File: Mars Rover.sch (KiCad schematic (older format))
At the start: 37 parts, among them J1 Barrel_Jack, SW1 KILLSWITCH

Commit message: Testing Commit
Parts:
- added D?: D_Schottky, symbol Device:D_Schottky
- added R?: R, symbol Device:R
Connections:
- net labels added: CHRG_VL
- wire segments 113 -> 115
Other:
- moved on the sheet: D?
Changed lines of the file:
@@
 Wire Wire Line
 	-5200 6100 -6300 6100
-Wire Wire Line
-	-5100 6050 -6500 6050
-Wire Wire Line
-	-6500 6050 -6500 6100
 $Comp
 L power:GND #PWR?
@@
 	-6300 6100 -6300 6450
 Connection ~ -6550 6450
-Wire Wire Line
-	-6500 5950 -6500 6050
-Connection ~ -6500 6050
 $Comp
 L Device:R R?
@@
 Connection ~ -2050 5200
 Wire Wire Line
-	-7350 4800 -2050 4800
-Wire Wire Line
 	-4100 5200 -2600 5200
 $Comp
@@
 L pspice:DIODE D?
 U 1 1 5C0E81FE
-P -3750 5550
-F 0 "D?" H -3750 5815 50  0000 C CNN
-F 1 "DIODE" H -3750 5724 50  0000 C CNN
-F 2 "" H -3750 5550 50  0001 C CNN
-F 3 "~" H -3750 5550 50  0001 C CNN
-	1    -3750 5550
-	1    0    0    -1
-$EndComp
-Wire Wire Line
-	-4100 5550 -3950 5550
+P -3600 5550
+F 0 "D?" H -3600 5815 50  0000 C CNN
+F 1 "DIODE" H -3600 5724 50  0000 C CNN
+F 2 "" H -3600 5550 50  0001 C CNN
+F 3 "~" H -3600 5550 50  0001 C CNN
+	1    -3600 5550
+	1    0    0    -1
+$EndComp
+Wire Wire Line
+	-4100 5550 -3800 5550
 $Comp
 L Device:C C?
@@
 Connection ~ -4000 6100
 Wire Wire Line
-	-3550 5550 -3400 5550
-Wire Wire Line
 	-3400 5550 -3400 5650
 Wire Wire Line
@@
 	-3750 6100 -3750 6850
 Wire Wire Line
-	-4000 6100 -3750 6100
+	-4000 6100 -3800 6100
 Wire Wire Line
 	-3750 6850 -3400 6850
@@
 Wire Wire Line
 	-2400 6950 -2400 6850
+Wire Wire Line
+	-6500 5950 -6500 6100
+Text Label -5450 6050 0    50   ~ 0
+CHRG_VL
+Wire Wire Line
+	-5100 6050 -5450 6050
+Text Label -4100 5550 0    50   ~ 0
+CHRG_VL
+Wire Wire Line
+	-7400 4800 -2050 4800
+$Comp
+L Device:D_Schottky D?
+U 1 1 5C0B3BF5
+P -3800 6250
+F 0 "D?" H -3800 6034 50  0000 C CNN
+F 1 "D_Schottky" H -3800 6125 50  0000 C CNN
+F 2 "" H -3800 6250 50  0001 C CNN
+F 3 "~" H -3800 6250 50  0001 C CNN
+	1    -3800 6250
+	0    1    1    0
+$EndComp
+Connection ~ -3800 6100
+Wire Wire Line
+	-3800 6100 -3750 6100
+Wire Wire Line
+	-4100 6350 -4100 6400
+Wire Wire Line
+	-4100 6400 -3850 6400
+$Comp
+L power:GND #PWR?
+U 1 1 5C0B7E2F
+P -3850 6400
+F 0 "#PWR?" H -3850 6150 50  0001 C CNN
+F 1 "GND" H -3845 6227 50  0000 C CNN
+F 2 "" H -3850 6400 50  0001 C CNN
+F 3 "" H -3850 6400 50  0001 C CNN
+	1    -3850 6400
+	1    0    0    -1
+$EndComp
+Connection ~ -3850 6400
+Wire Wire Line
+	-3850 6400 -3800 6400
+$Comp
+L Device:R R?
+U 1 1 5C0B8E08
+P -5700 2350
+F 0 "R?" H -5630 2396 50  0000 L CNN
+F 1 "R" H -5630 2305 50  0000 L CNN
+F 2 "" V -5770 2350 50  0001 C CNN
+F 3 "~" H -5700 2350 50  0001 C CNN
+	1    -5700 2350
+	1    0    0    -1
+$EndComp
 $EndSCHEMATC

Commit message: Battery Charger Done
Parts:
- added C?: 0.1uF, symbol Device:C
- C?: value CP1 -> 0.22uF
- C? (x2): value CP1 -> 22uF
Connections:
- net GND: now also C?.2
- net at U?.21 (CS): now also L?.2, C?.1

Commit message: Batteries done and raspi added
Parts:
- removed C? (x2): C, symbol Device:C
- removed C? (x7): 0.1uF, symbol Device:C
- removed C? (x3): 1nF, symbol Device:C
- removed C?: 1uF, symbol Device:C
- removed C?: CP1, symbol Device:CP1
- removed C?: 0.22uF, symbol Device:CP1
- removed C? (x2): 22uF, symbol Device:CP1
- removed D1, D2, D? (x2): D_Schottky, symbol Device:D_Schottky
- removed D? (x2): DIODE, symbol pspice:DIODE
- removed D? (x3): LED, symbol Device:LED
- removed L?: INDUCTOR, symbol pspice:INDUCTOR
- removed R? (x7): R, symbol Device:R
- removed R?: 10k, symbol Device:R
- removed R?: 0.05R, symbol Device:R
- removed U?: MAX1758, symbol Roverschemlib:MAX1758
- removed U?: Rpi0w, symbol Roverschemlib:Rpi0w
- added C?: 22uF, symbol Device:CP1
- added C?: 0.1uF, symbol Device:C
- added J?: Conn_01x03, symbol Connector_Generic:Conn_01x03
- added SW?: CHARGING, symbol Switch:SW_SPST
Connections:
- net +12V: now also SW?.2 (B); no longer SW1.1 (A)
- net GND: now also C?.1, C?.2
- net at J1.1: now also SW1.1 (A)
- net Buck5V/VIN renamed Battery Connection and Charge Management/VIN
- new net: C?.1, C?.2, J?.1 (Pin_1)
- new net Battery Connection and Charge Management/BATT_OUT: SW?.1 (A)
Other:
- note removed: "14.4V BATT IN HERE\n(PLUS CHARGING CKT)"
- note removed: "FASTCHG\n"
- note removed: "FAULT\n"
- note removed: "FULL CHARGE\n"
- note removed: "NOT 5VL, BUT ‘TO VL’"
- note removed: "VIN\n"
- note removed: "VOUT"
- moved on the sheet: J1, SW1

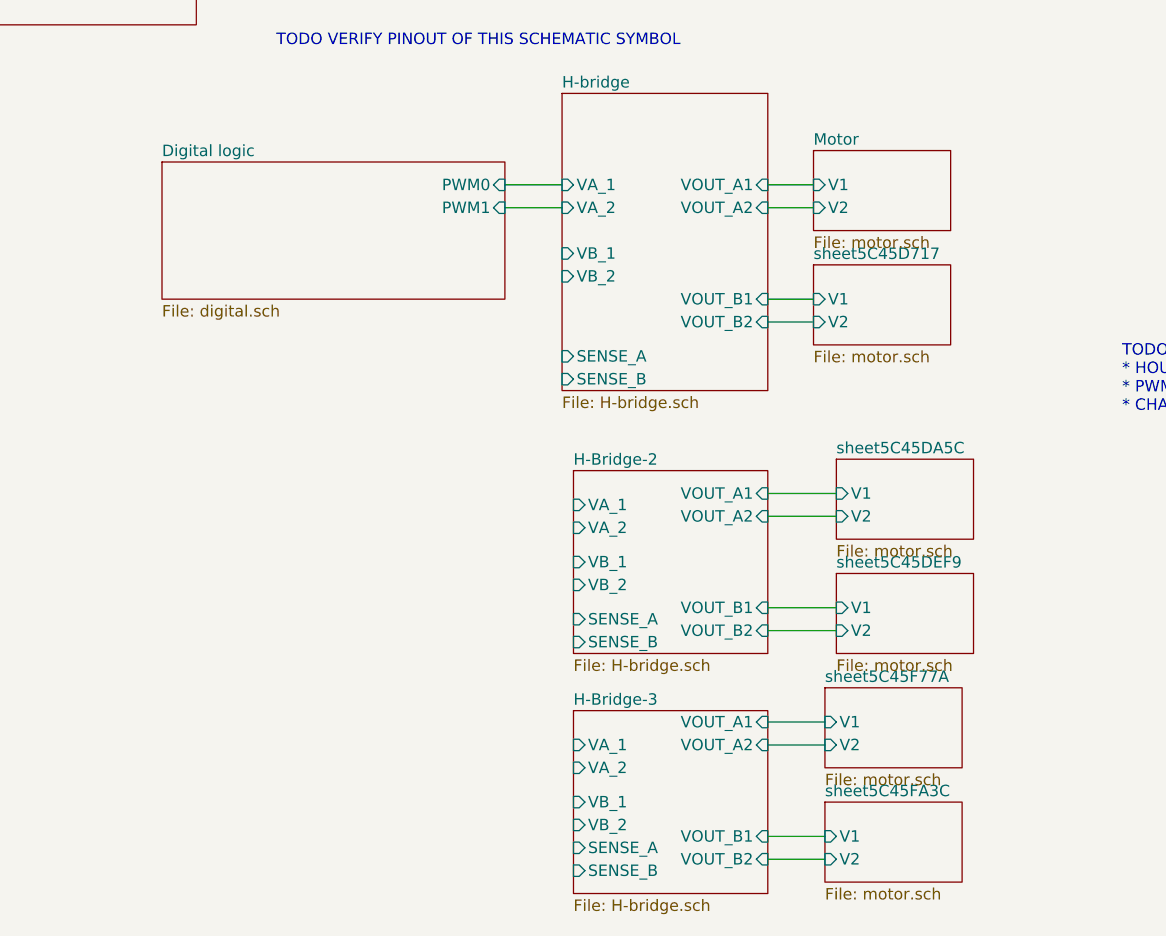
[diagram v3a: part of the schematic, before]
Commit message: Added housekeeping ADC, schematics almost done
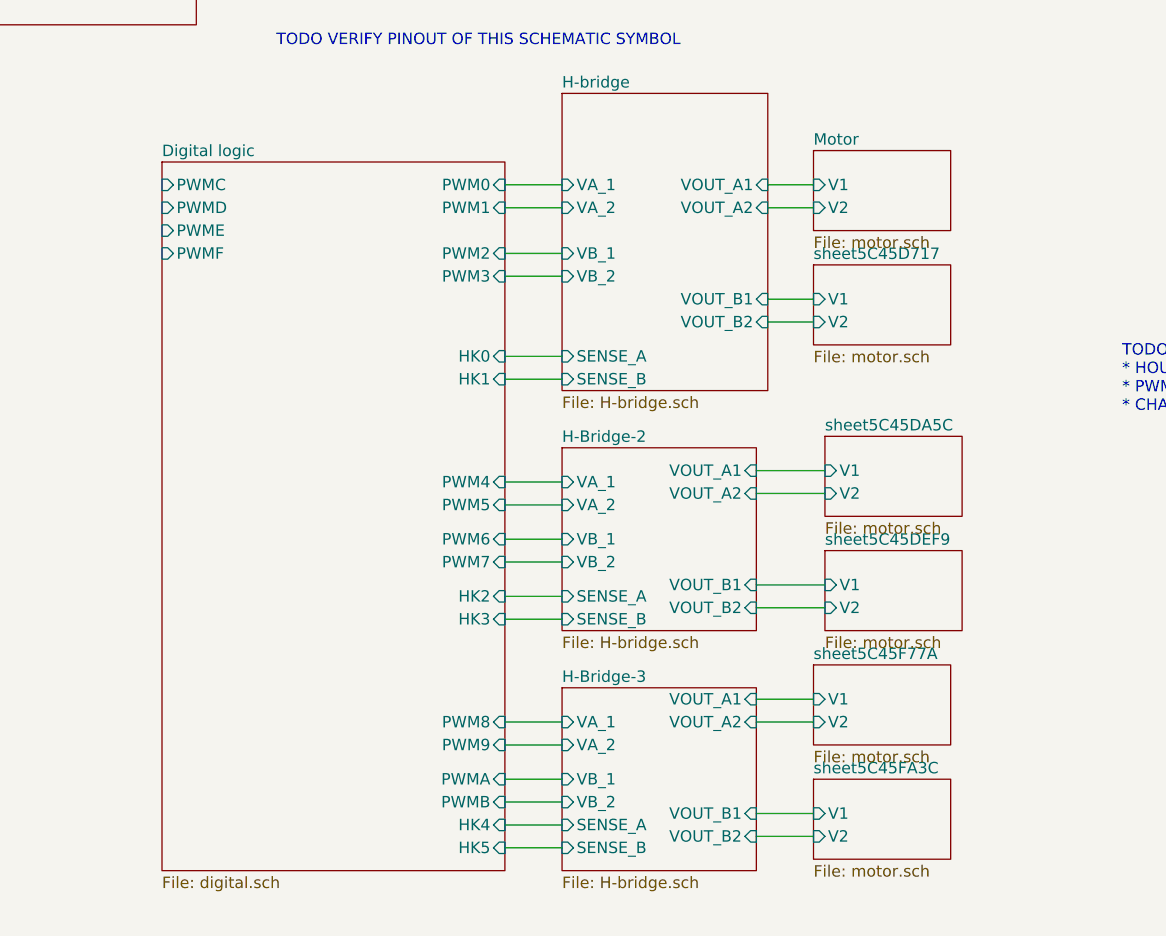
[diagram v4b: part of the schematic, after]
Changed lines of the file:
@@
 F0 "Motor" 50
 F1 "motor.sch" 50
-F3 "V1" I L 7000 3100 50
-F4 "V2" I L 7000 3200 50
-$EndSheet
-$Sheet
-S 5950 4350 850  800
+F2 "V1" I L 7000 3100 50
+F3 "V2" I L 7000 3200 50
+$EndSheet
+$Sheet
+S 5900 4250 850  800
 U 5BEEC4C8
 F0 "H-Bridge-2" 50
 F1 "H-bridge.sch" 50
-F2 "VOUT_B1" I R 6800 4950 50
-F3 "VOUT_B2" I R 6800 5050 50
-F4 "VOUT_A1" I R 6800 4450 50
-F5 "VOUT_A2" I R 6800 4550 50
-F6 "VB_1" I L 5950 4750 50
-F7 "VB_2" I L 5950 4850 50
-F8 "VA_1" I L 5950 4500 50
-F9 "VA_2" I L 5950 4600 50
-F10 "SENSE_B" I L 5950 5100 50
-F11 "SENSE_A" I L 5950 5000 50
-$EndSheet
-$Sheet
-S 5950 5400 850  800
+F2 "VOUT_B1" I R 6750 4850 50
+F3 "VOUT_B2" I R 6750 4950 50
+F4 "VOUT_A1" I R 6750 4350 50
+F5 "VOUT_A2" I R 6750 4450 50
+F6 "VB_1" I L 5900 4650 50
+F7 "VB_2" I L 5900 4750 50
+F8 "VA_1" I L 5900 4400 50
+F9 "VA_2" I L 5900 4500 50
+F10 "SENSE_B" I L 5900 5000 50
+F11 "SENSE_A" I L 5900 4900 50
+$EndSheet
+$Sheet
+S 5900 5300 850  800
 U 5BEEC636
 F0 "H-Bridge-3" 50
 F1 "H-bridge.sch" 50
-F2 "VOUT_B1" I R 6800 5950 50
-F3 "VOUT_B2" I R 6800 6050 50
-F4 "VOUT_A1" I R 6800 5450 50
-F5 "VOUT_A2" I R 6800 5550 50
-F6 "VB_1" I L 5950 5800 50
-F7 "VB_2" I L 5950 5900 50
-F8 "VA_1" I L 5950 5550 50
-F9 "VA_2" I L 5950 5650 50
-F10 "SENSE_B" I L 5950 6100 50
-F11 "SENSE_A" I L 5950 6000 50
+F2 "VOUT_B1" I R 6750 5850 50
+F3 "VOUT_B2" I R 6750 5950 50
+F4 "VOUT_A1" I R 6750 5350 50
+F5 "VOUT_A2" I R 6750 5450 50
+F6 "VB_1" I L 5900 5700 50
+F7 "VB_2" I L 5900 5800 50
+F8 "VA_1" I L 5900 5450 50
+F9 "VA_2" I L 5900 5550 50
+F10 "SENSE_B" I L 5900 6000 50
+F11 "SENSE_A" I L 5900 5900 50
 $EndSheet
 Text Notes 8350 4100 0    50   ~ 0
@@
 F0 "sheet5C45D717" 50
 F1 "motor.sch" 50
-F3 "V1" I L 7000 3600 50
-F4 "V2" I L 7000 3700 50
+F2 "V1" I L 7000 3600 50
+F3 "V2" I L 7000 3700 50
 $EndSheet
 Wire Wire Line
@@
 	6800 3700 7000 3700
 $Sheet
-S 7100 4300 600  350
+S 7050 4200 600  350
 U 5C45DA60
 F0 "sheet5C45DA5C" 50
 F1 "motor.sch" 50
-F3 "V1" I L 7100 4450 50
-F4 "V2" I L 7100 4550 50
-$EndSheet
-Wire Wire Line
-	7100 4450 6800 4450
-Wire Wire Line
-	6800 4550 7100 4550
-$Sheet
-S 7100 4800 600  350
+F2 "V1" I L 7050 4350 50
+F3 "V2" I L 7050 4450 50
+$EndSheet
+$Sheet
+S 7050 4700 600  350
 U 5C45DEFD
 F0 "sheet5C45DEF9" 50
 F1 "motor.sch" 50
-F3 "V1" I L 7100 4950 50
-F4 "V2" I L 7100 5050 50
-$EndSheet
-Wire Wire Line
-	7100 4950 6800 4950
-Wire Wire Line
-	6800 5050 7100 5050
-$Sheet
-S 7050 5300 600  350
+F2 "V1" I L 7050 4850 50
+F3 "V2" I L 7050 4950 50
+$EndSheet
+Wire Wire Line
+	7050 4850 6750 4850
+Wire Wire Line
+	6750 4950 7050 4950
+$Sheet
+S 7000 5200 600  350
 U 5C45F77E
 F0 "sheet5C45F77A" 50
 F1 "motor.sch" 50
-F3 "V1" I L 7050 5450 50
-F4 "V2" I L 7050 5550 50
-$EndSheet
-Wire Wire Line
-	7050 5450 6800 5450
-Wire Wire Line
-	6800 5550 7050 5550
-$Sheet
-S 7050 5800 600  350
+F2 "V1" I L 7000 5350 50
+F3 "V2" I L 7000 5450 50
+$EndSheet
+Wire Wire Line
+	7000 5350 6750 5350
+Wire Wire Line
+	6750 5450 7000 5450
+$Sheet
+S 7000 5700 600  350
 U 5C45FA40
 F0 "sheet5C45FA3C" 50
 F1 "motor.sch" 50
-F3 "V1" I L 7050 5950 50
-F4 "V2" I L 7050 6050 50
-$EndSheet
-Wire Wire Line
-	7050 5950 6800 5950
-Wire Wire Line
-	6800 6050 7050 6050
-$Sheet
-S 4150 3000 1500 600
+F2 "V1" I L 7000 5850 50
+F3 "V2" I L 7000 5950 50
+$EndSheet
+Wire Wire Line
+	7000 5850 6750 5850
+Wire Wire Line
+	6750 5950 7000 5950
+$Sheet
+S 4150 3000 1500 3100
 U 5C46155B
 F0 "Digital logic" 50
@@
 F2 "PWM0" I R 5650 3100 50
 F3 "PWM1" I R 5650 3200 50
+F4 "PWM2" I R 5650 3400 50
+F5 "PWM3" I R 5650 3500 50
+F6 "PWM4" I R 5650 4400 50
+F7 "PWM5" I R 5650 4500 50
+F8 "PWM6" I R 5650 4650 50
+F9 "PWM7" I R 5650 4750 50
+F10 "PWM8" I R 5650 5450 50
+F11 "PWM9" I R 5650 5550 50
+F12 "PWMA" I R 5650 5700 50
+F13 "PWMB" I R 5650 5800 50
+F14 "PWMC" I L 4150 3100 50
+F15 "PWMD" I L 4150 3200 50
+F16 "PWME" I L 4150 3300 50
+F17 "PWMF" I L 4150 3400 50
+F18 "HK0" I R 5650 3850 50
+F19 "HK1" I R 5650 3950 50
+F20 "HK2" I R 5650 4900 50
+F21 "HK3" I R 5650 5000 50
+F22 "HK4" I R 5650 5900 50
+F23 "HK5" I R 5650 6000 50
 $EndSheet
 $Comp
@@
 Wire Wire Line
 	5900 3200 5650 3200
+Wire Wire Line
+	5650 3400 5900 3400
+Wire Wire Line
+	5900 3500 5650 3500
+Wire Wire Line
+	5650 4400 5900 4400
+Wire Wire Line
+	5900 4500 5650 4500
+Wire Wire Line
+	5650 4650 5900 4650
+Wire Wire Line
+	5900 4750 5650 4750
+Wire Wire Line
+	5650 5450 5900 5450
+Wire Wire Line
+	5900 5550 5650 5550
+Wire Wire Line
+	5650 5700 5900 5700
+Wire Wire Line
+	5650 5800 5900 5800
+Wire Wire Line
+	6750 4350 7050 4350
+Wire Wire Line
+	7050 4450 6750 4450
+Wire Wire Line
+	5900 6000 5650 6000
+Wire Wire Line
+	5650 5900 5900 5900
+Wire Wire Line
+	5650 4900 5900 4900
+Wire Wire Line
+	5900 5000 5650 5000
+Wire Wire Line
+	5650 3950 5900 3950
+Wire Wire Line
+	5900 3850 5650 3850
 $EndSCHEMATC

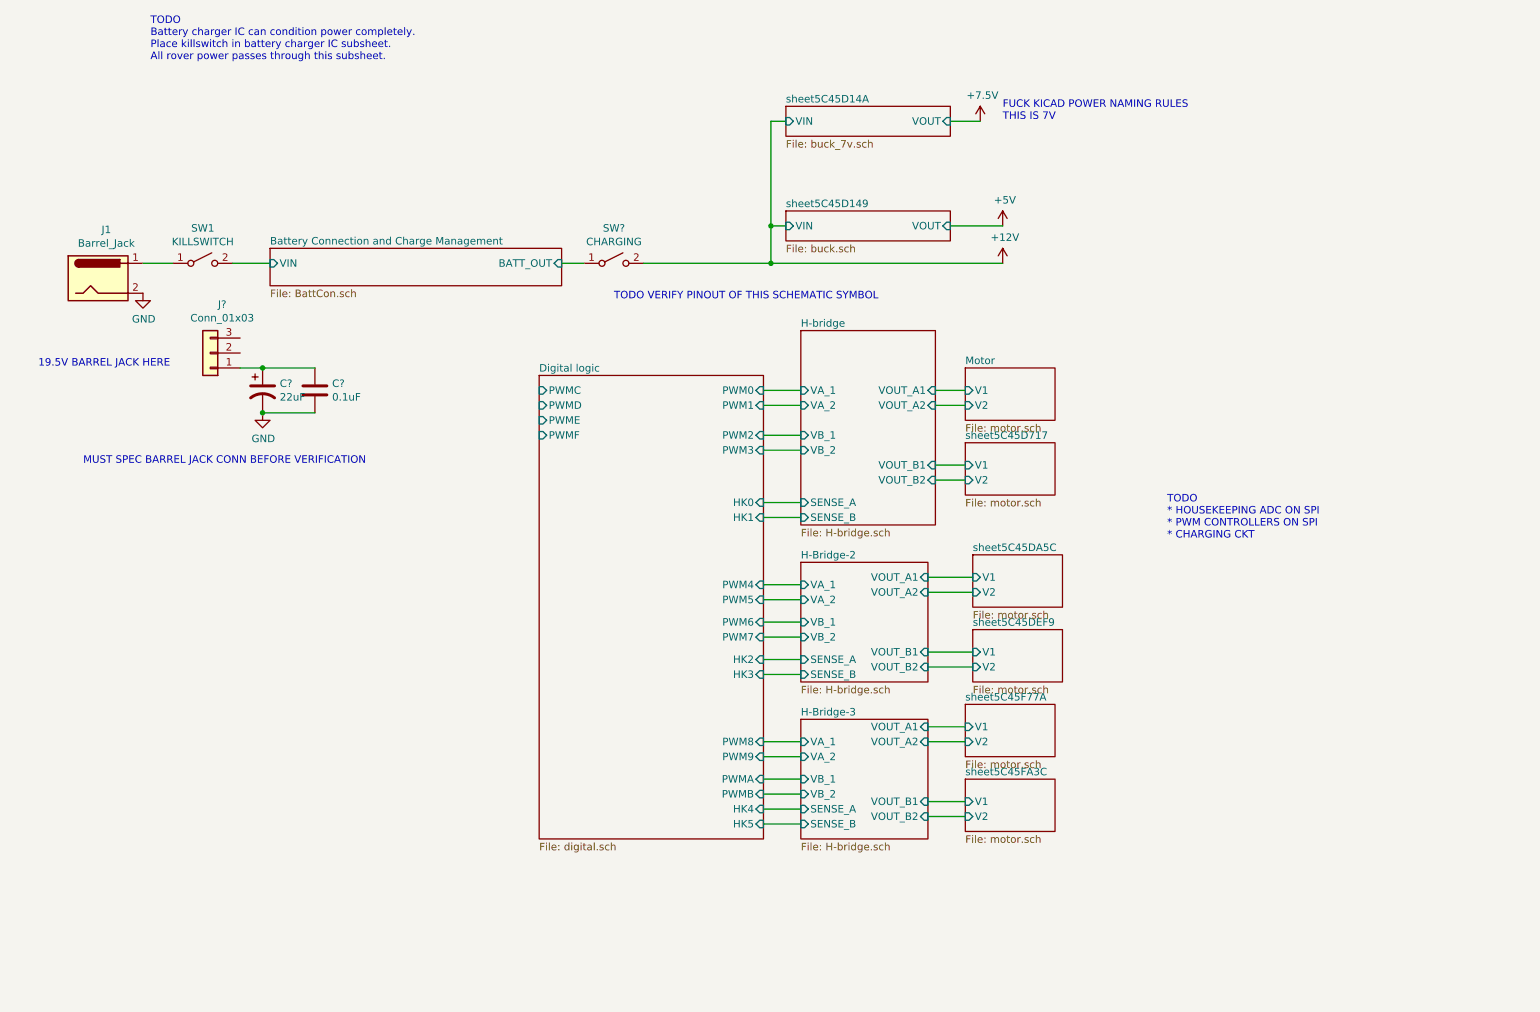
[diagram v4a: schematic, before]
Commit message: Schematics Done. Now need to do footprints
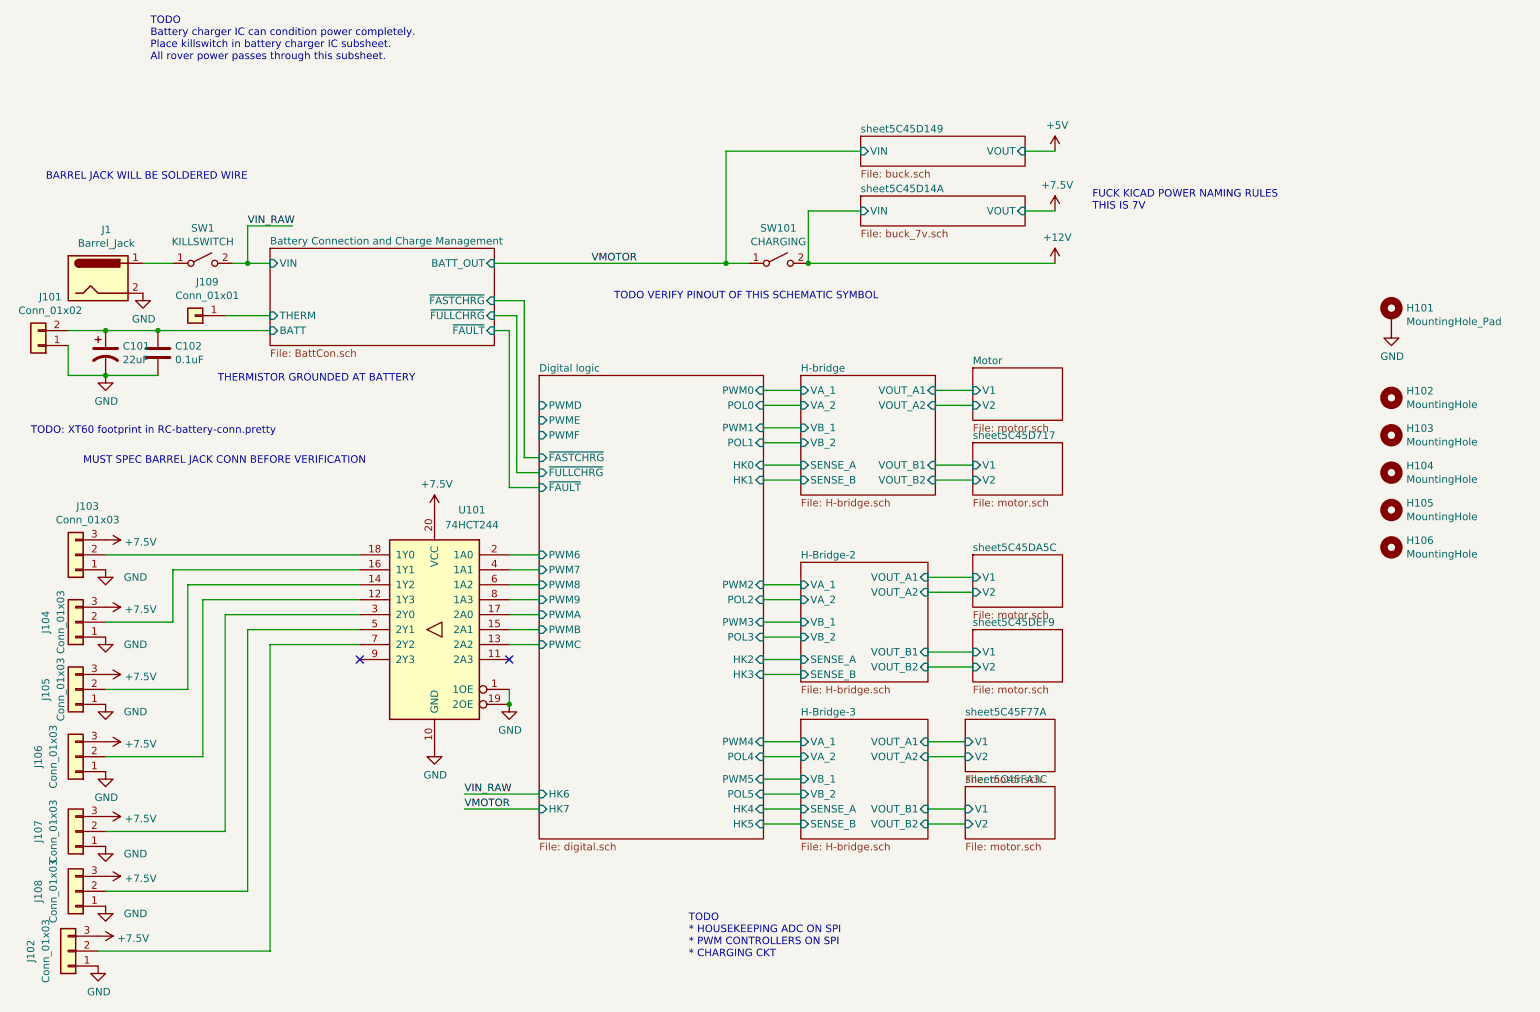
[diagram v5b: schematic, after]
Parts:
- removed J?: Conn_01x03, symbol Connector_Generic:Conn_01x03
- added H101: MountingHole_Pad, symbol Mechanical:MountingHole_Pad
- added H102, H103, H104, H105, H106: MountingHole, symbol Mechanical:MountingHole
- added J101: Conn_01x02, symbol Connector_Generic:Conn_01x02
- added J102, J103, J104, J105, J106, J107, J108: Conn_01x03, symbol Connector_Generic:Conn_01x03
- added J109: Conn_01x01, symbol Connector_Generic:Conn_01x01
- added U101: 74HCT244, symbol 74xx:74HCT244
- gave numbers to parts that had none: 3
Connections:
- net +7.5V: now also J102.3 (Pin_3), J103.3 (Pin_3), J104.3 (Pin_3), J105.3 (Pin_3), J106.3 (Pin_3), J107.3 (Pin_3), J108.3 (Pin_3), U101.20 (VCC)
- net Digital logic/PWM6: now also U101.2 (1A0)
- net Digital logic/PWM7: now also U101.4 (1A1)
- net Digital logic/PWM8: now also U101.6 (1A2)
- net Digital logic/PWM9: now also U101.8 (1A3)
- net Digital logic/PWMA: now also U101.17 (2A0)
- net Digital logic/PWMB: now also U101.15 (2A1)
- net Digital logic/PWMC: now also U101.13 (2A2)
- net GND: now also H101.1, J101.1 (Pin_1), J102.1 (Pin_1), J103.1 (Pin_1), J104.1 (Pin_1), J105.1 (Pin_1), J106.1 (Pin_1), J107.1 (Pin_1), J108.1 (Pin_1), U101.1 (1OE), U101.10 (GND), U101.19 (2OE)
- net Battery Connection and Charge Management/BATT: now reaches C101.1, C102.2
- net Battery Connection and Charge Management/BATT: now also J101.2 (Pin_2)
- net Battery Connection and Charge Management/BATT_OUT renamed VMOTOR
- net Battery Connection and Charge Management/VIN renamed VIN_RAW
- new net: J106.2 (Pin_2), U101.12 (1Y3)
- new net: J105.2 (Pin_2), U101.14 (1Y2)
- new net: J104.2 (Pin_2), U101.16 (1Y1)
- new net: J103.2 (Pin_2), U101.18 (1Y0)
- new net: J107.2 (Pin_2), U101.3 (2Y0)
- new net: J108.2 (Pin_2), U101.5 (2Y1)
- new net: J102.2 (Pin_2), U101.7 (2Y2)
- new net Battery Connection and Charge Management/THERM: J109.1 (Pin_1)
- no-connect marks 0 -> 2
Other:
- note added: "BARREL JACK WILL BE SOLDERED WIRE"
- note added: "THERMISTOR GROUNDED AT BATTERY"
- note added: "TODO: XT60 footprint in RC-battery-conn.pretty"
- note removed: "19.5V BARREL JACK HERE"
- moved on the sheet: C101, C102, SW101
